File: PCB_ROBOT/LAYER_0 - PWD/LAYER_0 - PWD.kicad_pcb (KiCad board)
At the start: 2 copper layers, 125 x 125 mm, 6 parts, among them J1 PRIMARY IN

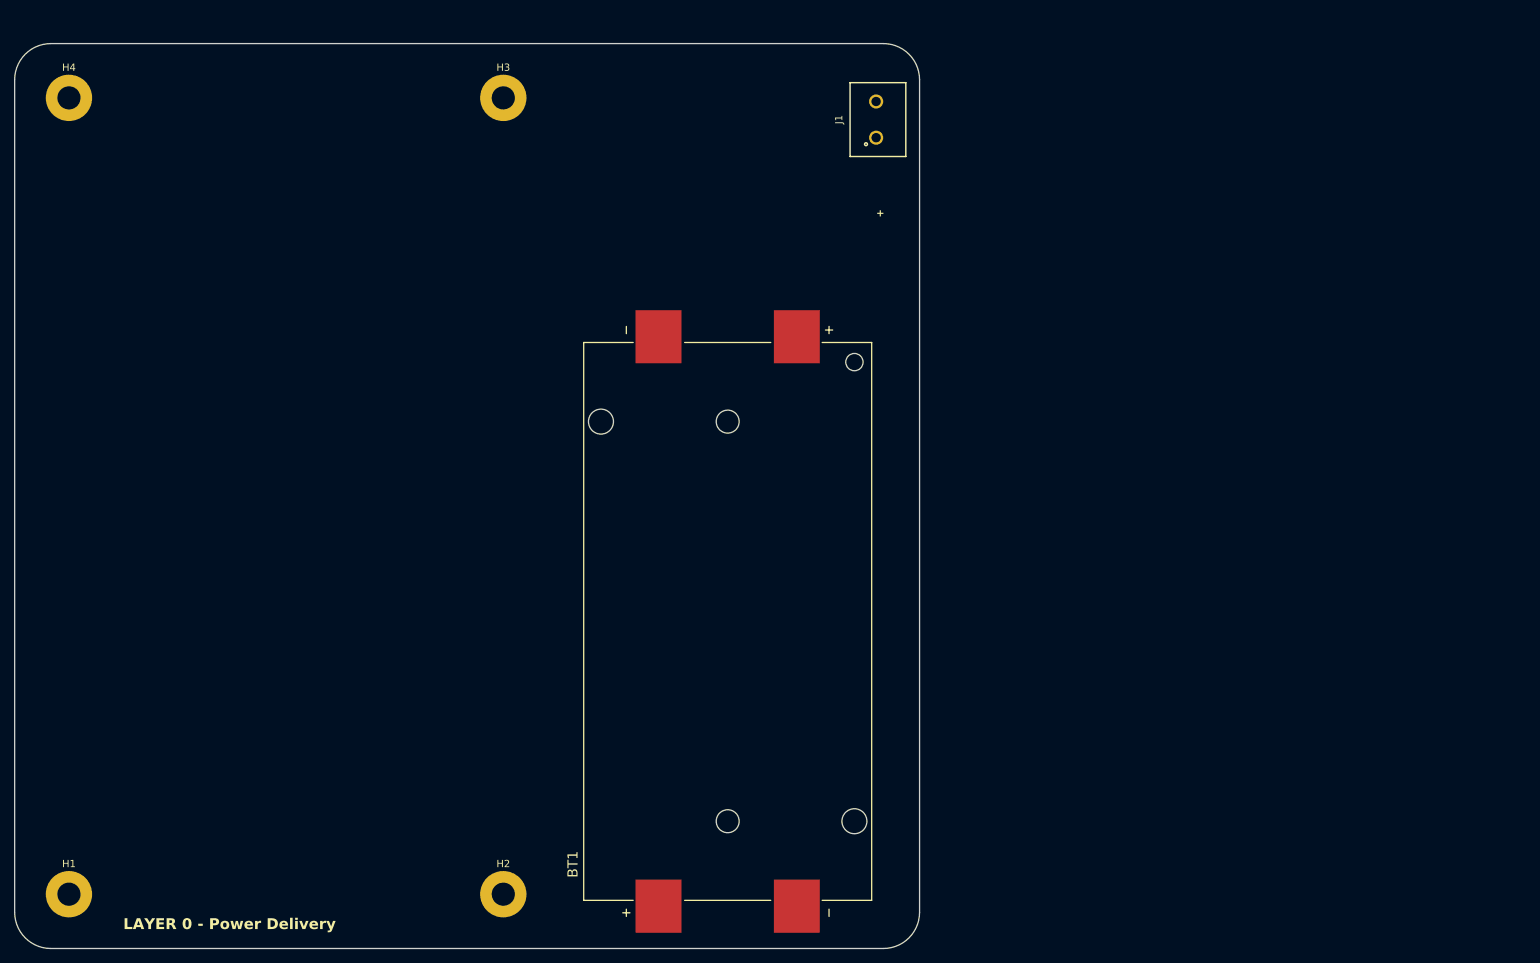
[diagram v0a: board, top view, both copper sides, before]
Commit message: 5v Integration
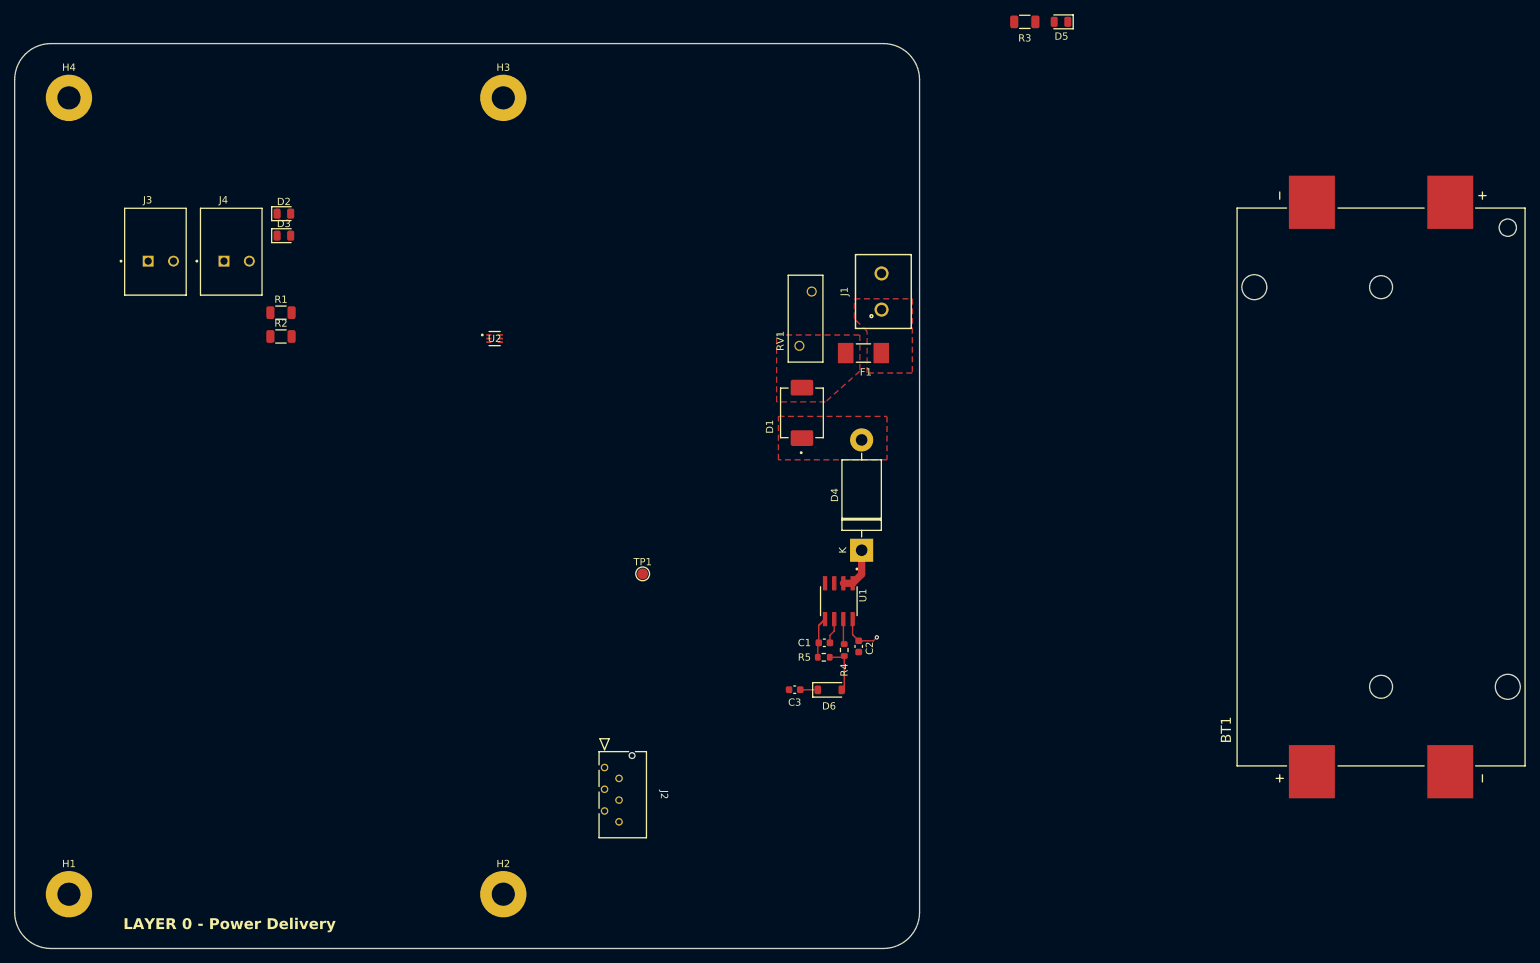
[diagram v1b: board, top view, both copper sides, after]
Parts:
- added C1: 0.1uF, Capacitor_SMD:C_0603_1608Metric, F.Cu at (146.8, 107.8)
- added C2: 0.1uF, Capacitor_SMD:C_0603_1608Metric, F.Cu at (151.6, 108.3)
- added C3: 0.1uF, Capacitor_SMD:C_0603_1608Metric, F.Cu at (142.8, 114.2)
- added D1: TVS, Footprints:DIOM7959X262N, F.Cu at (143.8, 76.0)
- added D2: green led, LED_SMD:LED_0805_2012Metric, F.Cu at (72.2, 48.5)
- added D3: green led, LED_SMD:LED_0805_2012Metric, F.Cu at (72.2, 51.5)
- added D4: 1N5404, Diode_THT:D_DO-201AD_P15.24mm_Horizontal, F.Cu at (152.0, 95.0)
- added D5: LED, LED_SMD:LED_0805_2012Metric, F.Cu at (179.5, 22.0)
- added D6: 1N4448W, Diode_SMD:D_SOD-123, F.Cu at (147.6, 114.3)
- added F1: Fuse, Footprints:FUSC6125X279N, F.Cu at (152.2, 67.8)
- added J2: 5031590600, Footprints:CON_5031590600_MOL, F.Cu at (116.5, 125.0)
- added J3: 12V_IN, Footprints:PHOENIX_1984963, F.Cu at (50.2, 59.8)
- added J4: 5V_IN, Footprints:PHOENIX_1984963, F.Cu at (60.7, 59.8)
- added R1: 450, Resistor_SMD:R_1206_3216Metric, F.Cu at (71.8, 62.2)
- added R2: 150, Resistor_SMD:R_1206_3216Metric, F.Cu at (71.8, 65.5)
- added R3: 2.7K, Resistor_SMD:R_1206_3216Metric, F.Cu at (174.5, 22.0)
- added R4: 2.2k, Resistor_SMD:R_0603_1608Metric, F.Cu at (149.6, 108.8)
- added R5: 2.2k, Resistor_SMD:R_0603_1608Metric, F.Cu at (146.8, 109.8)
- added RV1: B72210S0400K101, Footprints:VAR_B72210S0400K101, F.Cu at (144.2, 63.0)
- added TP1: TestPoint, TestPoint:TestPoint_Pad_D1.5mm, F.Cu at (121.8, 98.3)
- added U1: ACS712ELCTR-05B-T, Footprints:SOIC127P600X175-8N, F.Cu at (148.8, 102.0)
- added U2: TPS566247DRLR, Footprints:SOT-5X3-6_DRL_TEX, F.Cu at (101.3, 65.7)
- moved BT1 92.1 mm to (223.8, 86.2)
- moved J1 23.8 mm to (154.8, 59.2)
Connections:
- J1 pad 2: GNDREF -> GND
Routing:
- net Net-(D6-A): track 0.00 -> 6.89 mm
- net GND: track 0.00 -> 6.78 mm
- net Net-(D4-K): track 0.00 -> 6.35 mm
- net /5V_AUX: track 0.00 -> 6.05 mm, vias 0 -> 1
- net Net-(U1-FILTER): track 0.00 -> 3.52 mm
- net Net-(U1-VIOUT): track 0.00 -> 3.50 mm
- net /ISENSE_1: track 0.00 -> 2.43 mm
- added copper zone on F.Cu, net Net-(D1-PadA)
- added copper zone on F.Cu, net Net-(D4-A)
- added copper zone on F.Cu, net Net-(F1-Pad1)
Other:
- board text removed: "+"

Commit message: temp save/ partial traces prog
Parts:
- removed J2: 5031590600, Footprints:CON_5031590600_MOL
- added C10: 100nF, Capacitor_SMD:C_0603_1608Metric, F.Cu at (135.8, 93.5)
- added C11: 2.2uF, Capacitor_SMD:C_1210_3225Metric, F.Cu at (137.0, 100.5)
- added C12: 2.2uF, Capacitor_SMD:C_1210_3225Metric, F.Cu at (142.2, 100.5)
- added C13: 56nF, Capacitor_SMD:C_0603_1608Metric, F.Cu at (131.5, 82.2)
- added C14: 56nF, Capacitor_SMD:C_0603_1608Metric, F.Cu at (64.0, 82.4)
- added C15: 100nF, Capacitor_SMD:C_0603_1608Metric, F.Cu at (108.0, 83.5)
- added C16: 3pF, Capacitor_SMD:C_0805_2012Metric, F.Cu at (121.2, 79.2)
- added C17: 560pF, Resistor_SMD:R_0603_1608Metric, F.Cu at (128.3, 80.5)
- added C18: 8.2nF, Capacitor_SMD:C_0603_1608Metric, F.Cu at (132.2, 78.7)
- added C19: 620pF, Capacitor_SMD:C_0603_1608Metric, F.Cu at (132.7, 65.5)
- added C20: 4.7uF, Capacitor_SMD:C_1210_3225Metric, F.Cu at (122.5, 70.2)
- added C21: 4.7uF, Capacitor_SMD:C_1210_3225Metric, F.Cu at (123.5, 74.2)
- added C22: 4.7uF, Capacitor_SMD:C_1210_3225Metric, F.Cu at (111.5, 71.5)
- added C23: 22uF, Capacitor_SMD:C_0805_2012Metric, F.Cu at (117.8, 67.5)
- added C24: 22uF, Capacitor_SMD:C_0805_2012Metric, F.Cu at (117.8, 64.8)
- added C25: 22uF, Capacitor_SMD:C_0805_2012Metric, F.Cu at (118.8, 74.8)
- added C4: 10uF, Capacitor_SMD:C_0805_2012Metric, F.Cu at (130.8, 71.0)
- added C5: 10uF, Capacitor_SMD:C_0805_2012Metric, F.Cu at (129.0, 68.8)
- added C6: 100nF, Resistor_SMD:R_0603_1608Metric, F.Cu at (122.3, 67.5)
- added C7: 22uF, Capacitor_SMD:C_0805_2012Metric, F.Cu at (117.5, 70.0)
- added C8: 100nF, Capacitor_SMD:C_0603_1608Metric, F.Cu at (118.2, 72.5)
- added C9: 2.2uF, Capacitor_SMD:C_1210_3225Metric, F.Cu at (131.8, 100.5)
- added J5: V_I_SENSE, Footprints:17352658, F.Cu at (150.8, 132.2)
- added L2: IHLP6767DZER100M11, Footprints:INDPM172172X400N, F.Cu at (127.5, 50.2)
- added L3: XAL5030-222MEC, Footprints:XAL5030222MEC, F.Cu at (110.0, 62.0)
- added Q1: CSD19534Q5A, Footprints:TRANS_CSD19534Q5A, F.Cu at (125.9, 98.0)
- added Q2: CSD19532KTTT, 3d-files:CSD19536KTTT, F.Cu at (112.5, 100.2)
- added R10: 237k, Resistor_SMD:R_0603_1608Metric, F.Cu at (142.2, 95.5)
- added R11: 7.68k, Resistor_SMD:R_0603_1608Metric, F.Cu at (144.8, 91.6)
- added R12: 2.1k, Resistor_SMD:R_0603_1608Metric, F.Cu at (139.0, 95.6)
- added R13: 39.2k, Resistor_SMD:R_0603_1608Metric, F.Cu at (131.9, 84.2)
- added R14: 20k, Resistor_SMD:R_0603_1608Metric, F.Cu at (115.0, 81.5)
- added R15: 20k, Resistor_SMD:R_0603_1608Metric, F.Cu at (115.0, 79.5)
- added R16: 1.82k, Resistor_SMD:R_0805_2012Metric, F.Cu at (119.5, 92.2)
- added R17: 2.15k, Resistor_SMD:R_0603_1608Metric, F.Cu at (129.8, 77.8)
- added R18: 18k, Resistor_SMD:R_0603_1608Metric, F.Cu at (129.0, 73.8)
- added R19: 1.27k, Resistor_SMD:R_0603_1608Metric, F.Cu at (124.8, 81.8)
- added R20: 6.98, Resistor_SMD:R_0603_1608Metric, F.Cu at (129.0, 65.5)
- added R6: 100k, Resistor_SMD:R_0603_1608Metric, F.Cu at (107.0, 68.2)
- added R7: 14.3k, Resistor_SMD:R_0603_1608Metric, F.Cu at (103.2, 68.2)
- added R8: 220k, Resistor_SMD:R_0603_1608Metric, F.Cu at (113.8, 76.5)
- added R9: 30k, Resistor_SMD:R_0603_1608Metric, F.Cu at (110.2, 76.4)
- added TP2: VSENSE_1, TestPoint:TestPoint_Pad_D1.5mm, F.Cu at (140.2, 145.5)
- added U3: LM5146RGYR, Footprints:RGY0020B-MFG, F.Cu at (125.7, 86.2)
- TP1: value TestPoint -> ISENSE_1
- moved TP1 52.1 mm to (143.8, 145.5)
- moved U2 10.3 mm to (104.6, 75.5), turned to 180 degrees
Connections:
- net /PRIMARY_IN renamed /56V_PROTECTED
- J3 pad 1: /12V_LOCAL -> /12V_IN_5V_CONV
- R1 pad 1: /12V_LOCAL -> /12V_IN_5V_CONV
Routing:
- net GND: track 6.78 -> 104.5 mm, vias 0 -> 8
- net Net-(Q2-D): track 0.00 -> 96.6 mm, vias 0 -> 2
- net /ISENSE_1: track 2.43 -> 46.3 mm, vias 0 -> 2
- net /12V_IN_5V_CONV: track 0.00 -> 28.4 mm, vias 0 -> 2
- net Net-(U3-FB): track 0.00 -> 24.5 mm, vias 0 -> 2
- net Net-(U3-BST): track 0.00 -> 24.1 mm, vias 0 -> 2
- net /56V_PROTECTED: track 0.00 -> 23.5 mm
- net Net-(U3-EN_UVLO): track 0.00 -> 21.7 mm
- net Net-(U3-VCC): track 0.00 -> 20.4 mm, vias 0 -> 2
- net Net-(U3-VIN): track 0.00 -> 19.2 mm
- net Net-(U2-SW): track 0.00 -> 19.0 mm, vias 0 -> 2
- net Net-(U3-ILIM): track 0.00 -> 17.6 mm, vias 0 -> 2
- net Net-(U3-HO): track 0.00 -> 13.9 mm, vias 0 -> 2
- net Net-(U3-SYNCIN): track 0.00 -> 11.9 mm
- net Net-(Q2-G): track 0.00 -> 11.6 mm, vias 0 -> 2
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- added copper zone on F.Cu, net /12V_IN_5V_CONV
- added copper zone on F.Cu, net /56V_PROTECTED
- added copper zone on F.Cu, net /5V_5A
- added copper zone on F.Cu, net GND
- added copper zone on F.Cu, net Net-(Q2-D)
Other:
- board text added: "Disconnect FFC"
- board text added: "POWER MONITORISATION"
- board text added: "to read TP"
